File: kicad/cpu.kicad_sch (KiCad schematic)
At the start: 6 parts, among them U4 W65C02SxP, U5 AT28C256

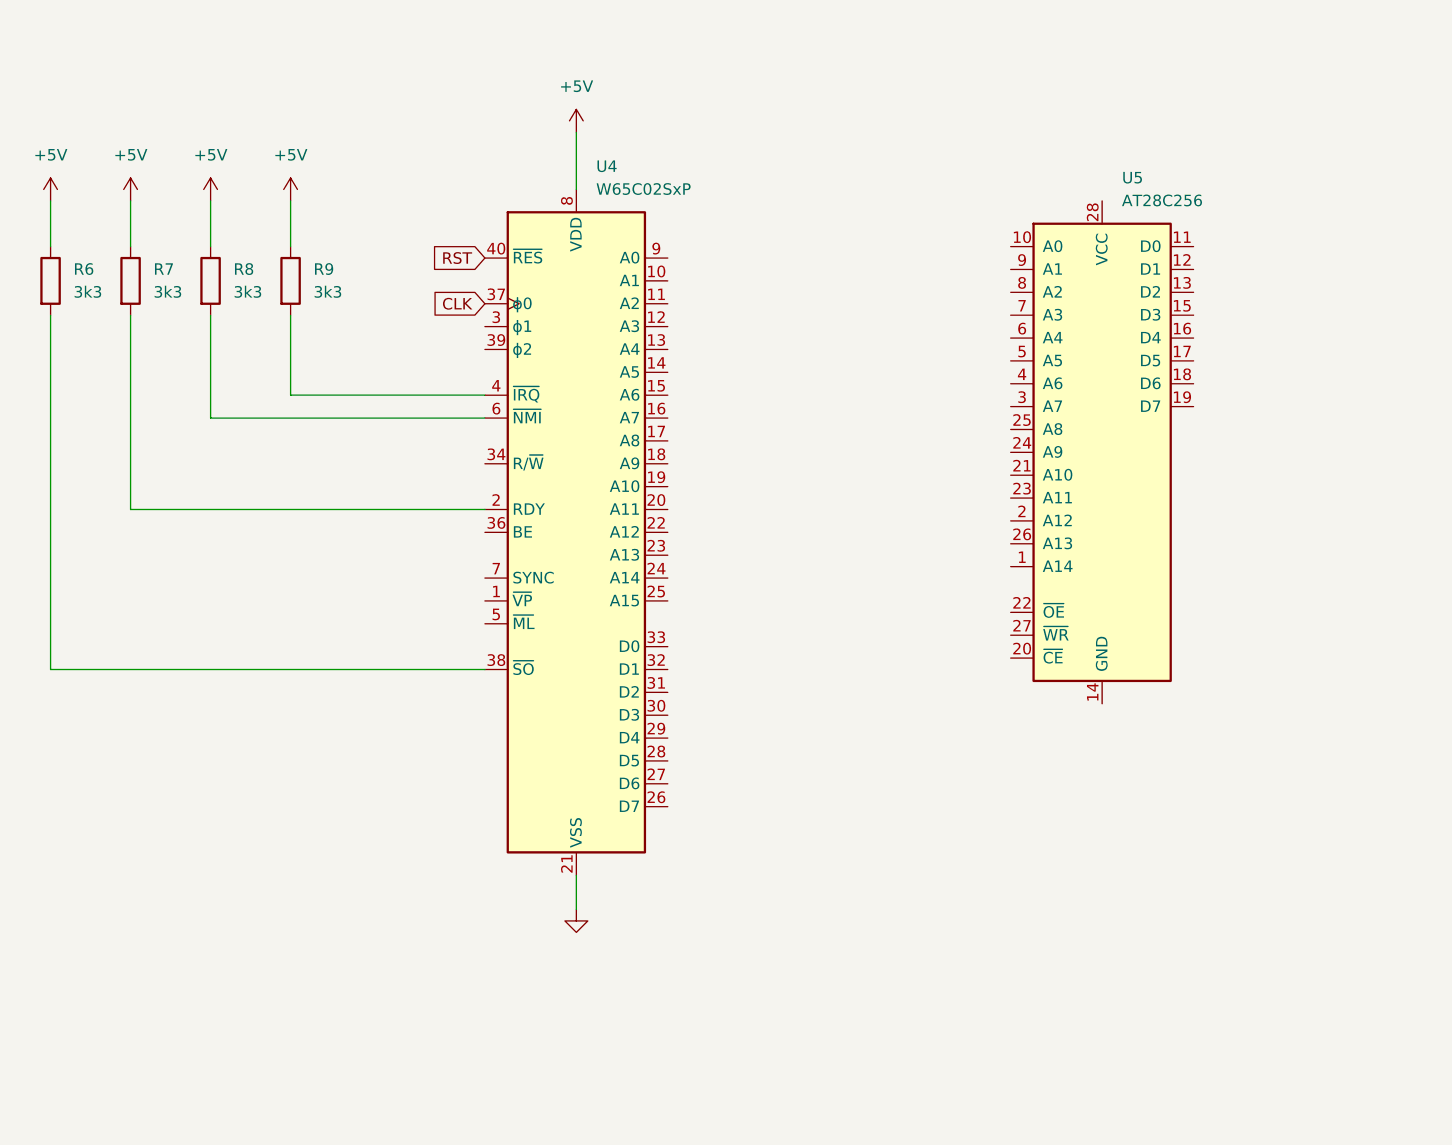
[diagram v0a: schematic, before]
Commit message: Wired up ROM memory
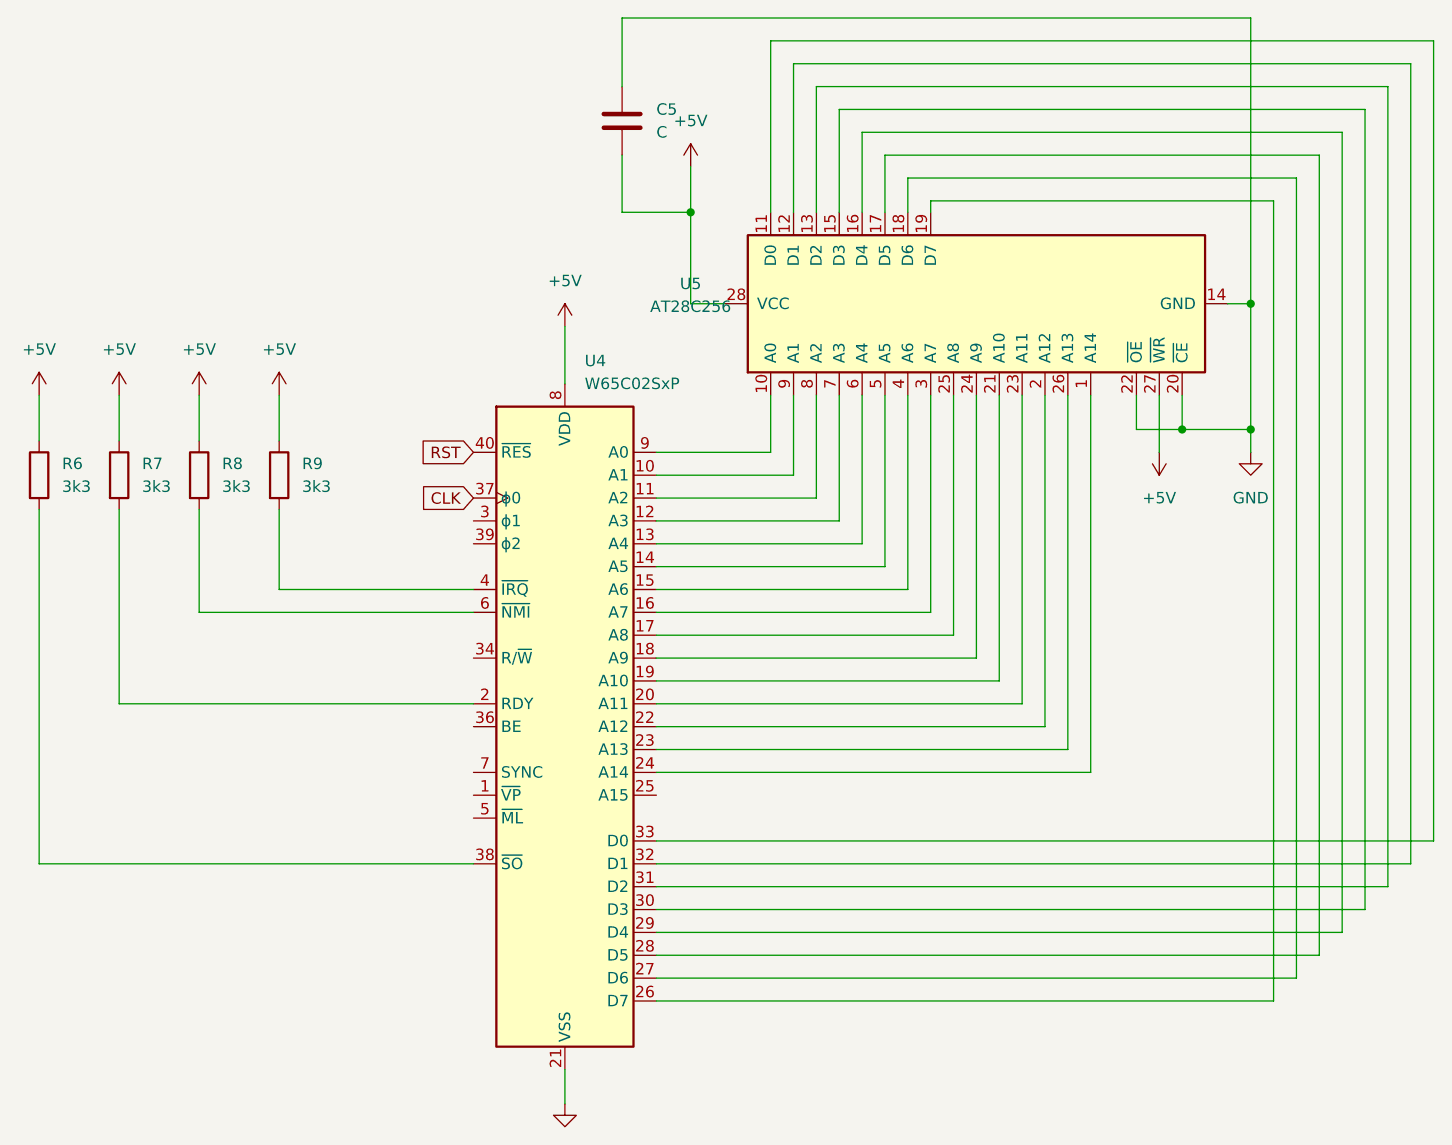
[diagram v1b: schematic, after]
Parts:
- added C5: C, symbol Device:C
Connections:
- net +5V: now also U5.27 (~{WR}), U5.28 (VCC), C5.1
- net GND: now also U5.14 (GND), U5.20 (~{CE}), U5.22 (~{OE}), C5.2
- net at U5.1 (A14): now also U4.24 (A14)
- net at U5.10 (A0): now also U4.9 (A0)
- net at U5.11 (D0): now also U4.33 (D0)
- net at U5.12 (D1): now also U4.32 (D1)
- net at U5.13 (D2): now also U4.31 (D2)
- net at U5.15 (D3): now also U4.30 (D3)
- net at U5.16 (D4): now also U4.29 (D4)
- net at U5.17 (D5): now also U4.28 (D5)
- net at U5.18 (D6): now also U4.27 (D6)
- net at U5.19 (D7): now also U4.26 (D7)
- net at U5.2 (A12): now also U4.22 (A12)
- net at U5.21 (A10): now also U4.19 (A10)
- net at U5.23 (A11): now also U4.20 (A11)
- net at U5.24 (A9): now also U4.18 (A9)
- net at U5.25 (A8): now also U4.17 (A8)
- net at U5.26 (A13): now also U4.23 (A13)
- net at U5.3 (A7): now also U4.16 (A7)
- net at U5.4 (A6): now also U4.15 (A6)
- net at U5.5 (A5): now also U4.14 (A5)
- net at U5.6 (A4): now also U4.13 (A4)
- net at U5.7 (A3): now also U4.12 (A3)
- net at U5.8 (A2): now also U4.11 (A2)
- net at U5.9 (A1): now also U4.10 (A1)
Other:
- moved on the sheet: R6, R7, R8, R9, U4, U5
